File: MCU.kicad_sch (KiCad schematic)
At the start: 34 parts, among them J1 GT-USB-7010I, SW1 BOOT0, SW6 Reset, U1 STM32F722RETx, U2 AMS1117-3.3, X1 32.768kHz 7pF, Y1 16MHz 10pF

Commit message: Continued additional minor cleanups
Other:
- note added: "Add ground protection for crystal in PCB"
- note added: "USB 2.0 impedance: 90 Ohms differential"
- note removed: "TODO: Ground protection for crystal"
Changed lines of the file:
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@@
 	(title_block
 		(title "MCU, Crystals, USB and Power")
-		(date "2024-10-12")
+		(date "2024-11-06")
 		(rev "1")
 		(company "Douglas P. Fields, Jr.")
 	)
 	(junction
-		(at 185.42 109.22)
-		(diameter 0)
-		(color 0 0 0 0)
-	)
-	(junction
 		(at 53.34 100.33)
 		(diameter 0)
@@
 	(wire
 		(pts
+			(xy 204.47 99.06) (xy 204.47 97.79)
+		)
+		(stroke
+			(width 0)
+			(type default)
+		)
+	)
+	(wire
+		(pts
 			(xy 83.82 113.03) (xy 118.11 113.03)
 		)
@@
 	(wire
 		(pts
-			(xy 182.88 109.22) (xy 185.42 109.22)
+			(xy 182.88 109.22) (xy 187.96 109.22)
 		)
 		(stroke
@@
 	(wire
 		(pts
-			(xy 185.42 109.22) (xy 185.42 110.49)
+			(xy 187.96 109.22) (xy 187.96 110.49)
 		)
 		(stroke
@@
 	(wire
 		(pts
-			(xy 204.47 97.79) (xy 204.47 100.33)
+			(xy 200.66 99.06) (xy 200.66 95.25)
 		)
 		(stroke
@@
 	(wire
 		(pts
+			(xy 200.66 99.06) (xy 204.47 99.06)
+		)
+		(stroke
+			(width 0)
+			(type default)
+		)
+	)
+	(wire
+		(pts
 			(xy 109.22 120.65) (xy 118.11 120.65)
 		)
@@
 	(wire
 		(pts
-			(xy 185.42 109.22) (xy 187.96 109.22)
-		)
-		(stroke
-			(width 0)
-			(type default)
-		)
-	)
-	(wire
-		(pts
 			(xy 250.19 83.82) (xy 236.22 83.82)
 		)
@@
 		)
 	)
-	(text "TODO: Ground protection\nfor crystal"
+	(text "Add ground protection\nfor crystal in PCB"
 		(exclude_from_sim no)
 		(at 75.184 133.858 0)
@@
 		)
 	)
+	(text "USB 2.0 impedance: 90 Ohms differential "
+		(exclude_from_sim no)
+		(at 191.008 79.756 0)
+		(effects
+			(font
+				(size 1.27 1.27)
+			)
+		)
+	)
 	(text "Power Supply"
 		(exclude_from_sim no)
@@
 	(text "ESD Protection"
 		(exclude_from_sim no)
-		(at 195.58 112.522 0)
+		(at 199.136 112.522 0)
 		(effects
 			(font
@@
 	(symbol
 		(lib_id "power:+3V3")
-		(at 204.47 100.33 180)
+		(at 200.66 95.25 0)
 		(unit 1)
 		(exclude_from_sim no)
@@
 		(fields_autoplaced yes)
 		(property "Reference" "#PWR013"
-			(at 204.47 96.52 0)
+			(at 200.66 99.06 0)
 			(effects
 				(font
@@
 		)
 		(property "Value" "+3V3"
-			(at 204.47 105.41 0)
+			(at 200.66 90.17 0)
 			(effects
 				(font
@@
 		)
 		(property "Footprint" ""
-			(at 204.47 100.33 0)
+			(at 200.66 95.25 0)
 			(effects
 				(font
@@
 		)
 		(property "Datasheet" ""
-			(at 204.47 100.33 0)
+			(at 200.66 95.25 0)
 			(effects
 				(font
@@
 		)
 		(property "Description" "Power symbol creates a global label with name \"+3V3\""
-			(at 204.47 100.33 0)
+			(at 200.66 95.25 0)
 			(effects
 				(font
@@
 	(symbol
 		(lib_id "power:GND")
-		(at 185.42 110.49 0)
+		(at 187.96 110.49 0)
 		(unit 1)
 		(exclude_from_sim no)
@@
 		(fields_autoplaced yes)
 		(property "Reference" "#PWR018"
-			(at 185.42 116.84 0)
+			(at 187.96 116.84 0)
 			(effects
 				(font
@@
 		)
 		(property "Value" "GND"
-			(at 185.42 115.57 0)
+			(at 187.96 115.57 0)
 			(effects
 				(font
@@
 		)
 		(property "Footprint" ""
-			(at 185.42 110.49 0)
+			(at 187.96 110.49 0)
 			(effects
 				(font
@@
 		)
 		(property "Datasheet" ""
-			(at 185.42 110.49 0)
+			(at 187.96 110.49 0)
 			(effects
 				(font
@@
 		)
 		(property "Description" "Power symbol creates a global label with name \"GND\" , ground"
-			(at 185.42 110.49 0)
+			(at 187.96 110.49 0)
 			(effects
 				(font
@@
 		)
 		(property "LCSC" ""
-			(at 185.42 110.49 0)
+			(at 187.96 110.49 0)
 			(effects
 				(font
@@
 		)
 		(property "DPFNOTES" ""
-			(at 185.42 110.49 0)
+			(at 187.96 110.49 0)
 			(effects
 				(font
@@
 		)
 		(property "DPFURL" ""
-			(at 185.42 110.49 0)
+			(at 187.96 110.49 0)
 			(effects
 				(font

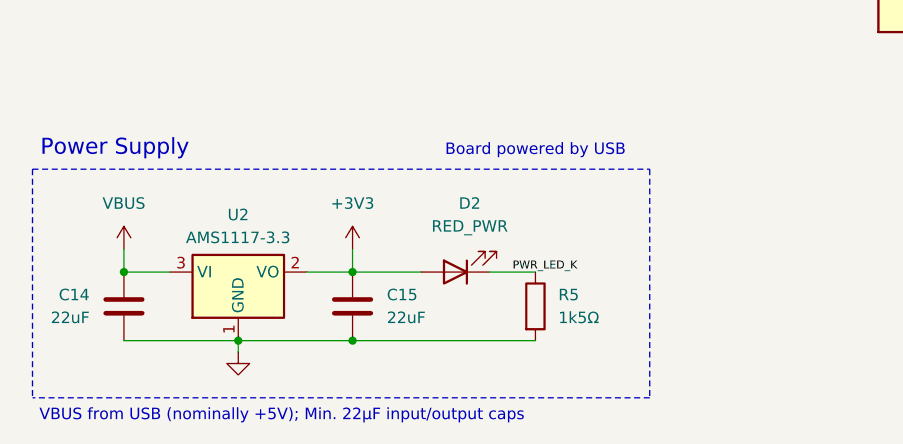
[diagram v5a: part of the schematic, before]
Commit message: Add 5V test pins
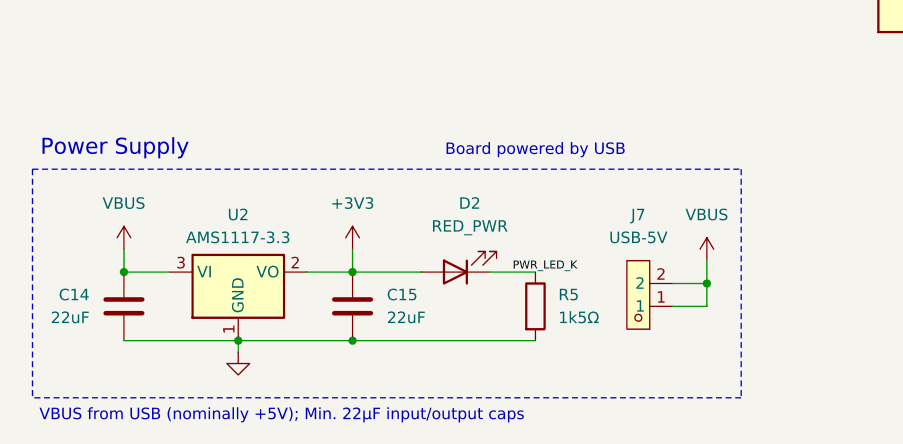
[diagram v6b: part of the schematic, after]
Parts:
- added J7: USB-5V, easyeda2kicad:HDR-TH_2P-P2.54-V-M-1, symbol easyeda2kicad:2541WV-02P
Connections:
- net VBUS: now also J7.1, J7.2
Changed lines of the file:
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@@
 	(title_block
 		(title "MCU, Crystals, USB and Power")
-		(date "2024-11-06")
+		(date "2024-11-10")
 		(rev "1")
 		(company "Douglas P. Fields, Jr.")
@@
 	)
 	(junction
+		(at 101.6 171.45)
+		(diameter 0)
+		(color 0 0 0 0)
+	)
+	(junction
 		(at 50.8 36.83)
 		(diameter 0)
@@
 	(polyline
 		(pts
-			(xy 95.25 184.15) (xy 26.67 184.15)
+			(xy 105.41 184.15) (xy 26.67 184.15)
 		)
 		(stroke
@@
 	(wire
 		(pts
+			(xy 101.6 171.45) (xy 101.6 168.91)
+		)
+		(stroke
+			(width 0)
+			(type default)
+		)
+	)
+	(wire
+		(pts
 			(xy 116.84 90.17) (xy 118.11 90.17)
 		)
@@
 	(wire
 		(pts
+			(xy 97.79 171.45) (xy 101.6 171.45)
+		)
+		(stroke
+			(width 0)
+			(type default)
+		)
+	)
+	(wire
+		(pts
 			(xy 195.58 99.06) (xy 195.58 100.33)
 		)
@@
 	(wire
 		(pts
+			(xy 97.79 173.99) (xy 101.6 173.99)
+		)
+		(stroke
+			(width 0)
+			(type default)
+		)
+	)
+	(wire
+		(pts
 			(xy 200.66 99.06) (xy 204.47 99.06)
 		)
@@
 	(polyline
 		(pts
-			(xy 95.25 158.75) (xy 95.25 184.15)
+			(xy 105.41 158.75) (xy 105.41 184.15)
 		)
 		(stroke
@@
 	(wire
 		(pts
+			(xy 101.6 173.99) (xy 101.6 171.45)
+		)
+		(stroke
+			(width 0)
+			(type default)
+		)
+	)
+	(wire
+		(pts
 			(xy 97.79 88.9) (xy 59.69 88.9)
 		)
@@
 	(polyline
 		(pts
-			(xy 26.67 158.75) (xy 95.25 158.75)
+			(xy 26.67 158.75) (xy 105.41 158.75)
 		)
 		(stroke
@@
 	)
 	(symbol
+		(lib_id "easyeda2kicad:2541WV-02P")
+		(at 92.71 172.72 180)
+		(unit 1)
+		(exclude_from_sim no)
+		(in_bom yes)
+		(on_board yes)
+		(dnp no)
+		(fields_autoplaced yes)
+		(property "Reference" "J7"
+			(at 93.98 163.83 0)
+			(effects
+				(font
+					(size 1.27 1.27)
+				)
+			)
+		)
+		(property "Value" "USB-5V"
+			(at 93.98 166.37 0)
+			(effects
+				(font
+					(size 1.27 1.27)
+				)
+			)
+		)
+		(property "Footprint" "easyeda2kicad:HDR-TH_2P-P2.54-V-M-1"
+			(at 92.71 163.83 0)
+			(effects
+				(font
+					(size 1.27 1.27)
+				)
+				(hide yes)
+			)
+		)
+		(property "Datasheet" ""
+			(at 92.71 172.72 0)
+			(effects
+				(font
+					(size 1.27 1.27)
+				)
+				(hide yes)
+			)
+		)
+		(property "Description" "2-pin 2.54mm male header, through hole"
+			(at 92.71 172.72 0)
+			(effects
+				(font
+					(size 1.27 1.27)
+				)
+				(hide yes)
+			)
+		)
+		(property "LCSC Part" "C5383111"
+			(at 92.71 161.29 0)
+			(effects
+				(font
+					(size 1.27 1.27)
+				)
+				(hide yes)
+			)
+		)
+		(property "LCSC" "C5383111"
+			(at 92.71 172.72 0)
+			(effects
+				(font
+					(size 1.27 1.27)
+				)
+				(hide yes)
+			)
+		)
+		(property "DPFNOTES" ""
+			(at 92.71 172.72 0)
+			(effects
+				(font
+					(size 1.27 1.27)
+				)
+				(hide yes)
+			)
+		)
+		(property "DPFURL" ""
+			(at 92.71 172.72 0)
+			(effects
+				(font
+					(size 1.27 1.27)
+				)
+				(hide yes)
+			)
+		)
+		(pin "1"
+		)
+		(pin "2"
+		)
+		(instances
+			(project ""
+				(path "/7cd74113-1f92-4dcc-8610-19aa9fc81e5f/fb10b81b-747c-4030-b31b-dec45474bc0e"
+					(reference "J7")
+					(unit 1)
+				)
+			)
+		)
+	)
+	(symbol
 		(lib_id "Device:C")
 		(at 77.47 40.64 0)
@@
 					(unit 1)
 				)
+			)
+		)
+	)
+	(symbol
+		(lib_id "power:VBUS")
+		(at 101.6 168.91 0)
+		(unit 1)
+		(exclude_from_sim no)
+		(in_bom yes)
+		(on_board yes)
+		(dnp no)
+		(fields_autoplaced yes)
+		(property "Reference" "#PWR040"
+			(at 101.6 172.72 0)
+			(effects
+				(font
+					(size 1.27 1.27)
+				)
+				(hide yes)
+			)
+		)
+		(property "Value" "VBUS"
+			(at 101.6 163.83 0)
+			(effects
+				(font
+					(size 1.27 1.27)
+				)
+			)
+		)
+		(property "Footprint" ""
+			(at 101.6 168.91 0)
+			(effects
+				(font
+					(size 1.27 1.27)
+				)
+				(hide yes)
+			)
+		)
+		(property "Datasheet" ""
+			(at 101.6 168.91 0)
+			(effects
+				(font
+					(size 1.27 1.27)
+				)
+				(hide yes)
+			)
+		)
+		(property "Description" "Power symbol creates a global label with name \"VBUS\""
+			(at 101.6 168.91 0)
+			(effects
+				(font
+					(size 1.27 1.27)
+				)
+				(hide yes)
+			)
+		)
+		(pin "1"
+		)
+		(instances
+			(project "stm-midi-poc1"
+				(path "/7cd74113-1f92-4dcc-8610-19aa9fc81e5f/fb10b81b-747c-4030-b31b-dec45474bc0e"
+					(reference "#PWR040")
+					(unit 1)
+				)

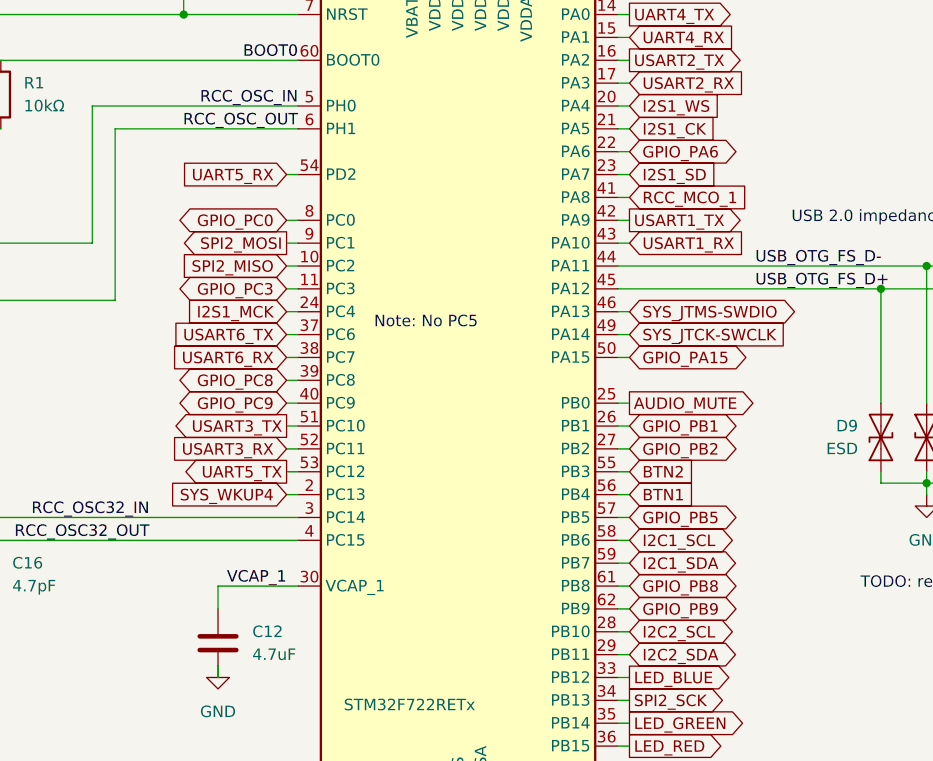
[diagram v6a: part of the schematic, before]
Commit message: More revisions for EVT2: 1. Move GAIN0/1 to MCU pins. 2. Revise SPI header with additional screen GPIO. 3. Revise GPIO header due to 1 and 2.
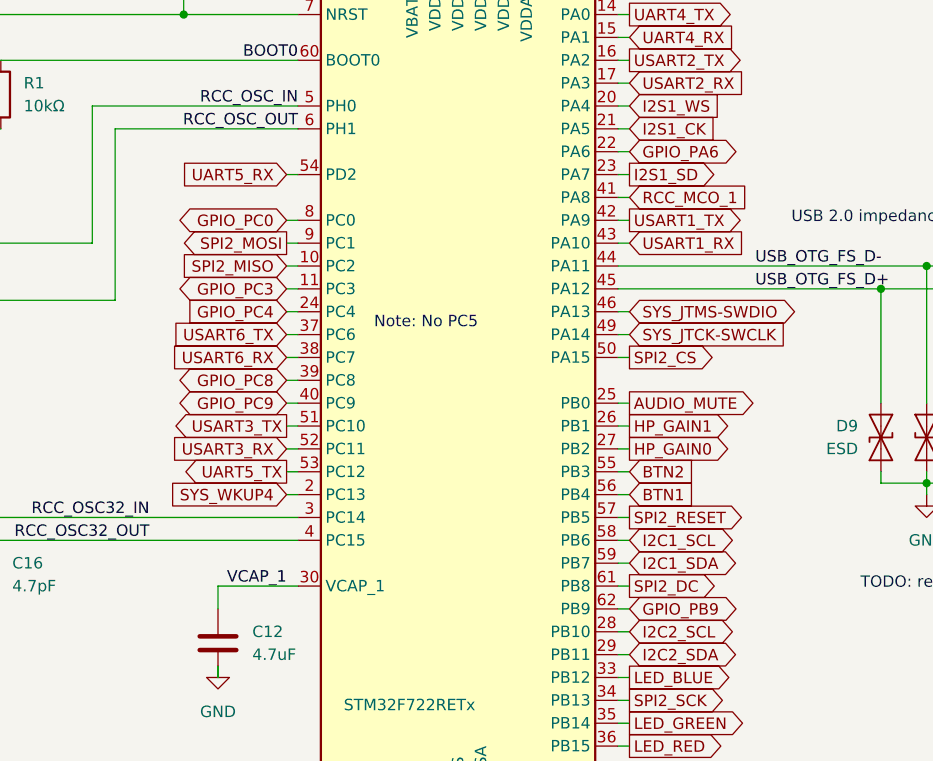
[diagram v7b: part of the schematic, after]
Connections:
- net GPIO_PA15 renamed SPI2_CS
- net GPIO_PB1 renamed HP_GAIN1
- net GPIO_PB2 renamed HP_GAIN0
- net GPIO_PB5 renamed SPI2_RESET
- net GPIO_PB8 renamed SPI2_DC
- net I2S1_MCK renamed GPIO_PC4
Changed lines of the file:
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@@
 		)
 	)
-	(global_label "I2S1_MCK"
+	(global_label "GPIO_PC4"
 		(shape input)
 		(at 116.84 90.17 180)
@@
 		)
 		(property "Intersheetrefs" "${INTERSHEET_REFS}"
-			(at 104.6625 90.17 0)
+			(at 104.6624 90.17 0)
 			(effects
 				(font
@@
 		)
 	)
-	(global_label "GPIO_PB1"
-		(shape bidirectional)
+	(global_label "HP_GAIN1"
+		(shape output)
 		(at 154.94 102.87 0)
 		(fields_autoplaced yes)
@@
 		)
 		(property "Intersheetrefs" "${INTERSHEET_REFS}"
-			(at 168.2289 102.87 0)
+			(at 166.9967 102.87 0)
 			(effects
 				(font
@@
 		)
 	)
-	(global_label "GPIO_PB2"
-		(shape bidirectional)
+	(global_label "HP_GAIN0"
+		(shape output)
 		(at 154.94 105.41 0)
 		(fields_autoplaced yes)
@@
 		)
 		(property "Intersheetrefs" "${INTERSHEET_REFS}"
-			(at 168.2289 105.41 0)
+			(at 166.9967 105.41 0)
 			(effects
 				(font
@@
 	)
 	(global_label "I2S1_SD"
-		(shape input)
+		(shape output)
 		(at 154.94 74.93 0)
 		(fields_autoplaced yes)
@@
 		)
 	)
-	(global_label "GPIO_PA15"
-		(shape bidirectional)
+	(global_label "SPI2_CS"
+		(shape output)
 		(at 154.94 95.25 0)
 		(fields_autoplaced yes)
@@
 		)
 		(property "Intersheetrefs" "${INTERSHEET_REFS}"
-			(at 169.257 95.25 0)
+			(at 165.6661 95.25 0)
 			(effects
 				(font
@@
 		)
 	)
-	(global_label "GPIO_PB5"
-		(shape bidirectional)
+	(global_label "SPI2_RESET"
+		(shape output)
 		(at 154.94 113.03 0)
 		(fields_autoplaced yes)
@@
 		)
 		(property "Intersheetrefs" "${INTERSHEET_REFS}"
-			(at 168.2289 113.03 0)
+			(at 168.9317 113.03 0)
 			(effects
 				(font
@@
 		)
 	)
-	(global_label "GPIO_PB8"
-		(shape bidirectional)
+	(global_label "SPI2_DC"
+		(shape output)
 		(at 154.94 120.65 0)
 		(fields_autoplaced yes)
@@
 		)
 		(property "Intersheetrefs" "${INTERSHEET_REFS}"
-			(at 168.2289 120.65 0)
-			(effects
-				(font
+			(at 165.7266 120.65 0)
+			(effects
+				(font
